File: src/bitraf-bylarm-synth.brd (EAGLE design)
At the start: 48.6 x 49.5 mm, 26 parts, among them IC1 LM386M-1, IC2 40106

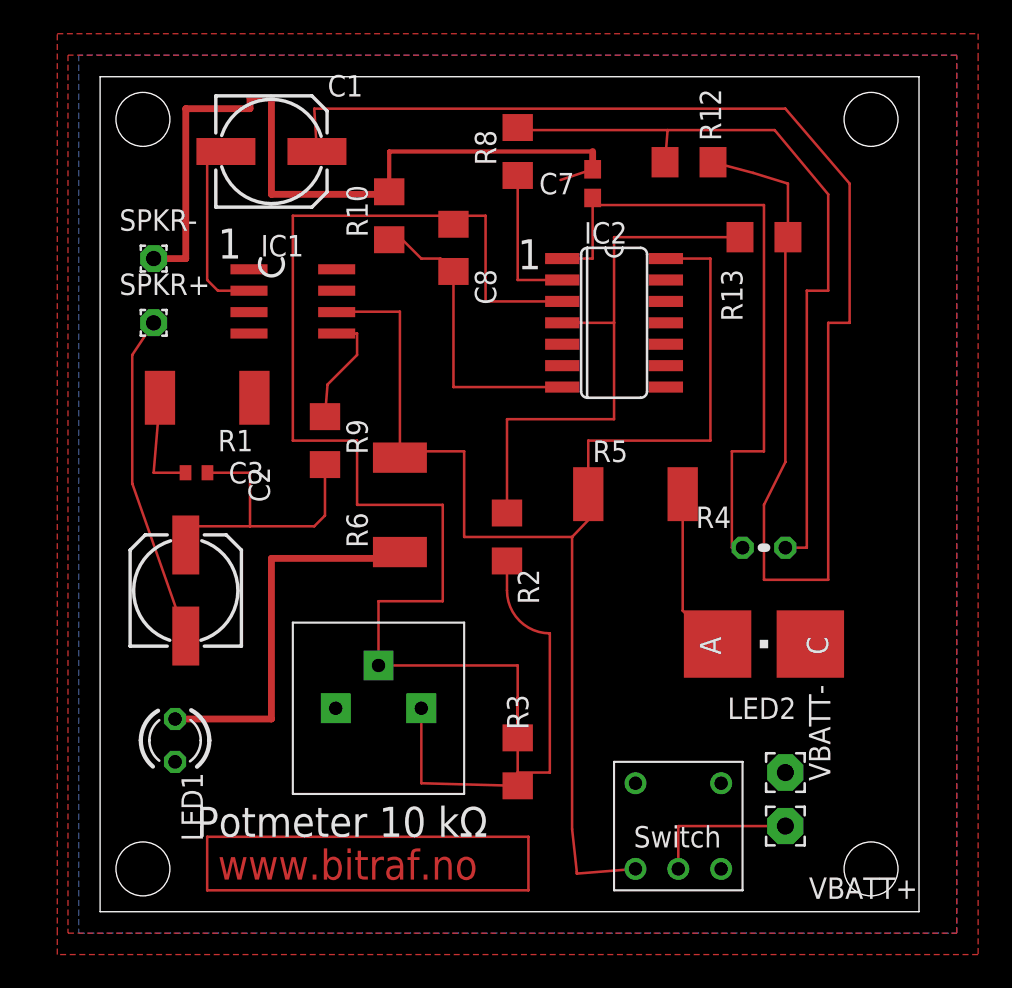
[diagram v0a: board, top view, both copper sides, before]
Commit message: Tweak schematics and layout for actual values used
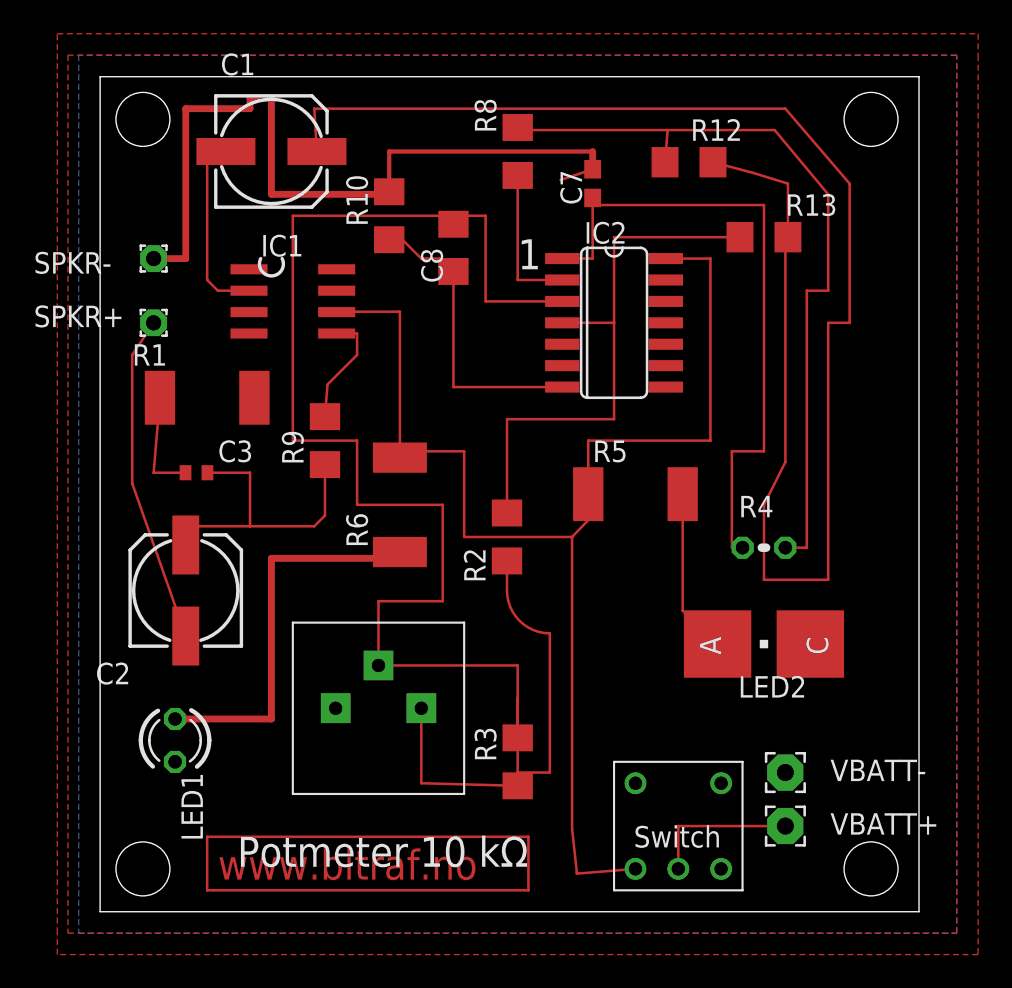
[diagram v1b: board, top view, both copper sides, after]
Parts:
- R3: value 1,5 kΩ -> 1,8 kΩ
- R5, R6: value 220Ω -> 270Ω
- R8: value 1,5 kΩ -> 100 Ω
